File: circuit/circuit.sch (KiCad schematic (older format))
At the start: 8 parts

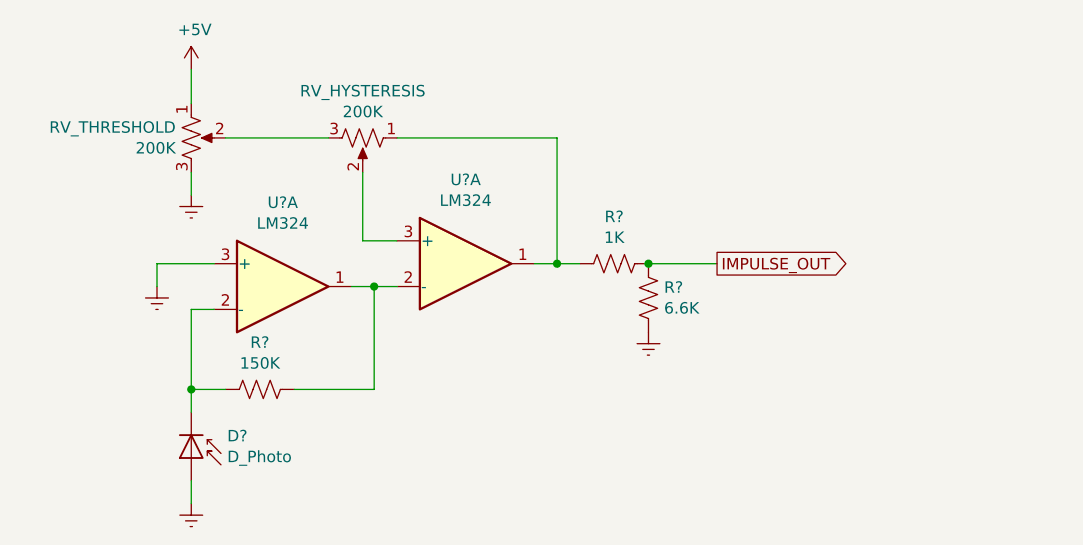
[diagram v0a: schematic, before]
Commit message: Update schematic.
Remove the hysteresis selection pot and change it to fixed 0.28v of hysteresis.
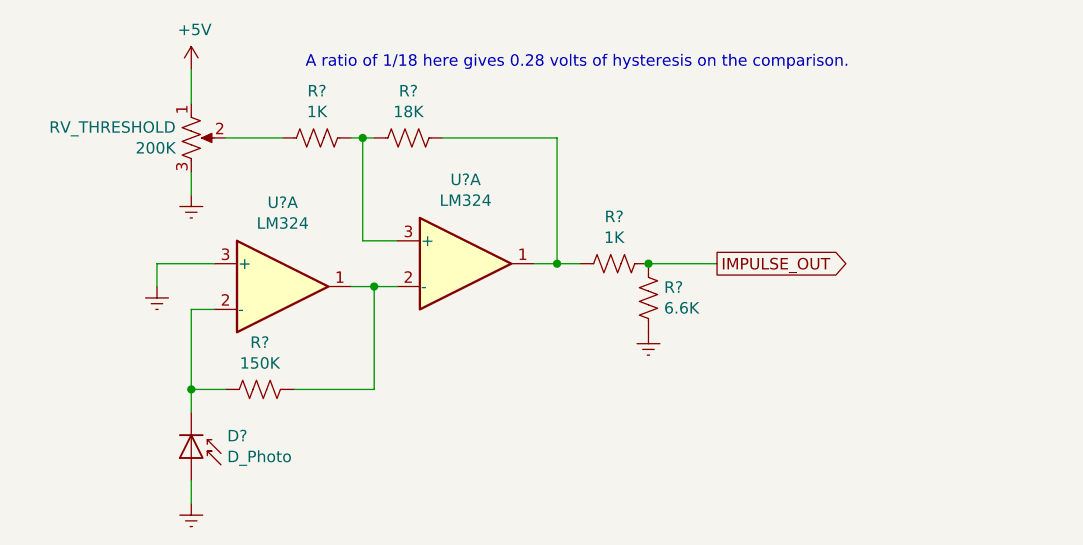
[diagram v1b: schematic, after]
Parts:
- removed RV_HYSTERESIS: 200K, symbol Device:R_POT_US
- added R?: 18K, symbol Device:R_US
- added R?: 1K, symbol Device:R_US
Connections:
- net at R?.2, U?.1: now also R?.2
- net at U?.3 (+): now also R?.1, R?.2
- net at RV_THRESHOLD.2: now also R?.1
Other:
- note added: "A ratio of 1/18 here gives 0.28 volts of hysteresis on the comparison."
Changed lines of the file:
@@
-$EndComp
-$Comp
-L Device:R_POT_US RV_HYSTERESIS
-U 1 1 61420C5A
-P 3700 1700
-F 0 "RV_HYSTERESIS" V 3495 1700 50  0000 C CNN
-F 1 "200K" V 3586 1700 50  0000 C CNN
-F 2 "" H 3700 1700 50  0001 C CNN
-F 3 "~" H 3700 1700 50  0001 C CNN
-	1    3700 1700
-	0    1    1    0
 $EndComp
 $Comp
@@
 	1    0    0    -1
 $EndComp
-Wire Wire Line
-	3100 1700 3550 1700
 $Comp
 L power:+5V #PWR?
@@
 	2950 1400 2950 1550
 Wire Wire Line
-	3850 1700 4550 1700
-Wire Wire Line
 	4550 1700 4550 2250
 Wire Wire Line
 	4550 2250 4450 2250
-Wire Wire Line
-	3700 1850 3700 2150
 Wire Wire Line
 	3700 2150 3850 2150
@@
 	3850 2350 3750 2350
 Connection ~ 3750 2350
+$Comp
+L Device:R_US R?
+U 1 1 61440E5A
+P 3900 1700
+F 0 "R?" V 4105 1700 50  0000 C CNN
+F 1 "18K" V 4014 1700 50  0000 C CNN
+F 2 "" V 3940 1690 50  0001 C CNN
+F 3 "~" H 3900 1700 50  0001 C CNN
+	1    3900 1700
+	0    -1   -1   0
+$EndComp
+Wire Wire Line
+	3700 1700 3700 2150
+$Comp
+L Device:R_US R?
+U 1 1 6144199F
+P 3500 1700
+F 0 "R?" V 3705 1700 50  0000 C CNN
+F 1 "1K" V 3614 1700 50  0000 C CNN
+F 2 "" V 3540 1690 50  0001 C CNN
+F 3 "~" H 3500 1700 50  0001 C CNN
+	1    3500 1700
+	0    -1   -1   0
+$EndComp
+Wire Wire Line
+	3650 1700 3700 1700
+Wire Wire Line
+	3700 1700 3750 1700
+Connection ~ 3700 1700
+Wire Wire Line
+	4050 1700 4550 1700
+Wire Wire Line
+	3350 1700 3100 1700
+Text Notes 3450 1400 0    50   ~ 0
+A ratio of 1/18 here gives 0.28 volts of hysteresis on the comparison.
 $EndSCHEMATC

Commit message: Add start of board layout
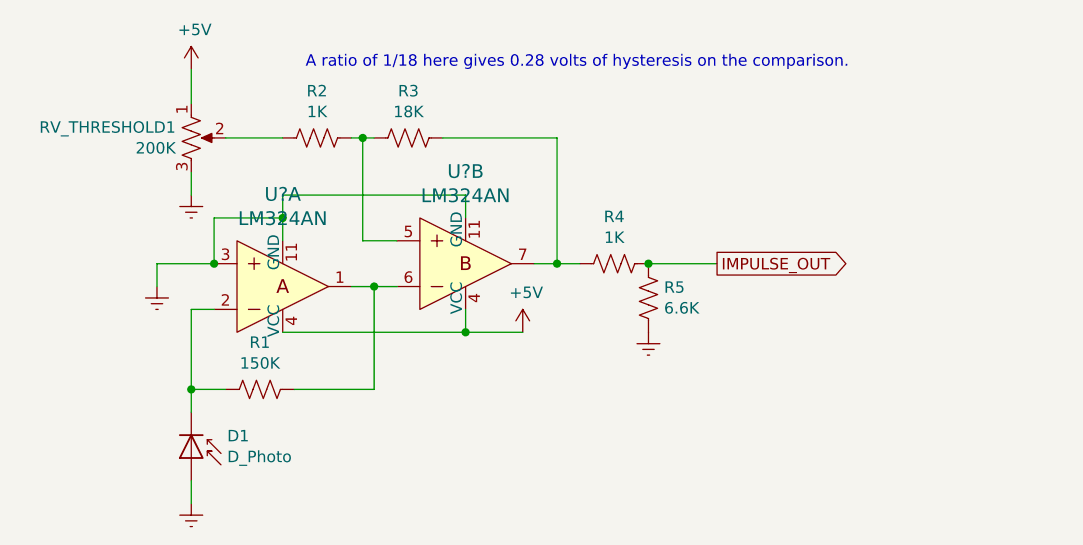
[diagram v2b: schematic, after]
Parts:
- removed U? (x2): LM324, symbol Amplifier_Operational:LM324
- added U? (x2): LM324AN, digikey-footprints:DIP-14_W3mm, symbol dk_Linear-Amplifiers-Instrumentation-OP-Amps-Buffer-Amps:LM324AN
- R1, R2, R3, R4, R5: renamed from R?; footprint (none) -> Resistor_THT:R_Axial_DIN0207_L6.3mm_D2.5mm_P10.16mm_Horizontal
- gave numbers to parts that had none: 1
- renumbered RV_THRESHOLD to RV_THRESHOLD1
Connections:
- net +5V: now also U?.4 (VCC), U?.4 (VCC)
- net Earth: now also U?.11 (GND), U?.11 (GND), U?.3
- net at R3.2, R4.2: now also U?.7
- net at R1.2: now also U?.1, U?.6
- net at R2.2, R3.1: now also U?.5
- net at D1.1 (K), R1.1: now also U?.2
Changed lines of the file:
@@
 $EndDescr
 $Comp
-L Amplifier_Operational:LM324 U?
-U 1 1 6141E584
-P 4150 2250
-F 0 "U?" H 4150 2617 50  0000 C CNN
-F 1 "LM324" H 4150 2526 50  0000 C CNN
-F 2 "" H 4100 2350 50  0001 C CNN
-F 3 "http://www.ti.com/lit/ds/symlink/lm2902-n.pdf" H 4200 2450 50  0001 C CNN
-	1    4150 2250
-	1    0    0    -1
-$EndComp
-$Comp
-L Device:R_POT_US RV_THRESHOLD
+L Device:R_POT_US RV_THRESHOLD1
 U 1 1 61422150
 P 2950 1700
-F 0 "RV_THRESHOLD" H 2882 1746 50  0000 R CNN
+F 0 "RV_THRESHOLD1" H 2882 1746 50  0000 R CNN
 F 1 "200K" H 2882 1655 50  0000 R CNN
 F 2 "" H 2950 1700 50  0001 C CNN
@@
 $EndComp
 $Comp
-L power:+5V #PWR?
+L power:+5V #PWR0101
 U 1 1 61423494
 P 2950 1400
-F 0 "#PWR?" H 2950 1250 50  0001 C CNN
+F 0 "#PWR0101" H 2950 1250 50  0001 C CNN
 F 1 "+5V" H 2965 1573 50  0000 C CNN
 F 2 "" H 2950 1400 50  0001 C CNN
@@
 $EndComp
 $Comp
-L power:Earth #PWR?
+L power:Earth #PWR0102
 U 1 1 6142409F
 P 2950 1950
-F 0 "#PWR?" H 2950 1700 50  0001 C CNN
+F 0 "#PWR0102" H 2950 1700 50  0001 C CNN
 F 1 "Earth" H 2950 1800 50  0001 C CNN
 F 2 "" H 2950 1950 50  0001 C CNN
@@
 Wire Wire Line
 	3700 2150 3850 2150
-$Comp
-L Amplifier_Operational:LM324 U?
-U 1 1 61425B46
-P 3350 2350
-F 0 "U?" H 3350 2717 50  0000 C CNN
-F 1 "LM324" H 3350 2626 50  0000 C CNN
-F 2 "" H 3300 2450 50  0001 C CNN
-F 3 "http://www.ti.com/lit/ds/symlink/lm2902-n.pdf" H 3400 2550 50  0001 C CNN
-	1    3350 2350
-	1    0    0    -1
-$EndComp
 Wire Wire Line
 	3650 2350 3750 2350
@@
 	2800 2250 2800 2350
 $Comp
-L power:Earth #PWR?
+L power:Earth #PWR0103
 U 1 1 61429E2B
 P 2800 2350
-F 0 "#PWR?" H 2800 2100 50  0001 C CNN
+F 0 "#PWR0103" H 2800 2100 50  0001 C CNN
 F 1 "Earth" H 2800 2200 50  0001 C CNN
 F 2 "" H 2800 2350 50  0001 C CNN
@@
 $EndComp
 $Comp
-L Device:R_US R?
+L Device:R_US R1
 U 1 1 6142A93A
 P 3250 2800
-F 0 "R?" V 3455 2800 50  0000 C CNN
+F 0 "R1" V 3455 2800 50  0000 C CNN
 F 1 "150K" V 3364 2800 50  0000 C CNN
-F 2 "" V 3290 2790 50  0001 C CNN
+F 2 "Resistor_THT:R_Axial_DIN0207_L6.3mm_D2.5mm_P10.16mm_Horizontal" V 3290 2790 50  0001 C CNN
 F 3 "~" H 3250 2800 50  0001 C CNN
 	1    3250 2800
@@
 	2950 2450 3050 2450
 $Comp
-L Device:D_Photo D?
+L Device:D_Photo D1
 U 1 1 6142C863
 P 2950 3100
-F 0 "D?" V 2854 3257 50  0000 L CNN
+F 0 "D1" V 2854 3257 50  0000 L CNN
 F 1 "D_Photo" V 2945 3257 50  0000 L CNN
 F 2 "" H 2900 3100 50  0001 C CNN
@@
 	2950 3200 2950 3300
 $Comp
-L power:Earth #PWR?
+L power:Earth #PWR0104
 U 1 1 6142D9DD
 P 2950 3300
-F 0 "#PWR?" H 2950 3050 50  0001 C CNN
+F 0 "#PWR0104" H 2950 3050 50  0001 C CNN
 F 1 "Earth" H 2950 3150 50  0001 C CNN
 F 2 "" H 2950 3300 50  0001 C CNN
@@
 $EndComp
 $Comp
-L Device:R_US R?
+L Device:R_US R4
 U 1 1 6142F1A5
 P 4800 2250
-F 0 "R?" V 4595 2250 50  0000 C CNN
+F 0 "R4" V 4595 2250 50  0000 C CNN
 F 1 "1K" V 4686 2250 50  0000 C CNN
-F 2 "" V 4840 2240 50  0001 C CNN
+F 2 "Resistor_THT:R_Axial_DIN0207_L6.3mm_D2.5mm_P10.16mm_Horizontal" V 4840 2240 50  0001 C CNN
 F 3 "~" H 4800 2250 50  0001 C CNN
 	1    4800 2250
@@
 $EndComp
 $Comp
-L Device:R_US R?
+L Device:R_US R5
 U 1 1 6142FDA4
 P 4950 2400
-F 0 "R?" H 4882 2354 50  0000 R CNN
+F 0 "R5" H 4882 2354 50  0000 R CNN
 F 1 "6.6K" H 4882 2445 50  0000 R CNN
-F 2 "" V 4990 2390 50  0001 C CNN
+F 2 "Resistor_THT:R_Axial_DIN0207_L6.3mm_D2.5mm_P10.16mm_Horizontal" V 4990 2390 50  0001 C CNN
 F 3 "~" H 4950 2400 50  0001 C CNN
 	1    4950 2400
@@
 $EndComp
 $Comp
-L power:Earth #PWR?
+L power:Earth #PWR0105
 U 1 1 6143068F
 P 4950 2550
-F 0 "#PWR?" H 4950 2300 50  0001 C CNN
+F 0 "#PWR0105" H 4950 2300 50  0001 C CNN
 F 1 "Earth" H 4950 2400 50  0001 C CNN
 F 2 "" H 4950 2550 50  0001 C CNN
@@
 Connection ~ 3750 2350
 $Comp
-L Device:R_US R?
+L Device:R_US R3
 U 1 1 61440E5A
 P 3900 1700
-F 0 "R?" V 4105 1700 50  0000 C CNN
+F 0 "R3" V 4105 1700 50  0000 C CNN
 F 1 "18K" V 4014 1700 50  0000 C CNN
-F 2 "" V 3940 1690 50  0001 C CNN
+F 2 "Resistor_THT:R_Axial_DIN0207_L6.3mm_D2.5mm_P10.16mm_Horizontal" V 3940 1690 50  0001 C CNN
 F 3 "~" H 3900 1700 50  0001 C CNN
 	1    3900 1700
@@
 	3700 1700 3700 2150
 $Comp
-L Device:R_US R?
+L Device:R_US R2
 U 1 1 6144199F
 P 3500 1700
-F 0 "R?" V 3705 1700 50  0000 C CNN
+F 0 "R2" V 3705 1700 50  0000 C CNN
 F 1 "1K" V 3614 1700 50  0000 C CNN
-F 2 "" V 3540 1690 50  0001 C CNN
+F 2 "Resistor_THT:R_Axial_DIN0207_L6.3mm_D2.5mm_P10.16mm_Horizontal" V 3540 1690 50  0001 C CNN
 F 3 "~" H 3500 1700 50  0001 C CNN
 	1    3500 1700
@@
 Text Notes 3450 1400 0    50   ~ 0
 A ratio of 1/18 here gives 0.28 volts of hysteresis on the comparison.
+$Comp
+L dk_Linear-Amplifiers-Instrumentation-OP-Amps-Buffer-Amps:LM324AN U?
+U 1 1 61447FCC
+P 3350 2350
+F 0 "U?" H 3350 1947 60  0000 C CNN
+F 1 "LM324AN" H 3350 2053 60  0000 C CNN
+F 2 "digikey-footprints:DIP-14_W3mm" H 3550 2550 60  0001 L CNN
+F 3 "http://www.ti.com/general/docs/suppproductinfo.tsp?distId=10&gotoUrl=http%3A%2F%2Fwww.ti.com%2Flit%2Fgpn%2Flm224" H 3550 2650 60  0001 L CNN
+F 4 "296-9542-5-ND" H 3550 2750 60  0001 L CNN "Digi-Key_PN"
+F 5 "LM324AN" H 3550 2850 60  0001 L CNN "MPN"
+F 6 "Integrated Circuits (ICs)" H 3550 2950 60  0001 L CNN "Category"
+F 7 "Linear - Amplifiers - Instrumentation, OP Amps, Buffer Amps" H 3550 3050 60  0001 L CNN "Family"
+F 8 "http://www.ti.com/general/docs/suppproductinfo.tsp?distId=10&gotoUrl=http%3A%2F%2Fwww.ti.com%2Flit%2Fgpn%2Flm224" H 3550 3150 60  0001 L CNN "DK_Datasheet_Link"
+F 9 "/product-detail/en/texas-instruments/LM324AN/296-9542-5-ND/412056" H 3550 3250 60  0001 L CNN "DK_Detail_Page"
+F 10 "IC OPAMP GP 4 CIRCUIT 14DIP" H 3550 3350 60  0001 L CNN "Description"
+F 11 "Texas Instruments" H 3550 3450 60  0001 L CNN "Manufacturer"
+F 12 "Active" H 3550 3550 60  0001 L CNN "Status"
+	1    3350 2350
+	1    0    0    1
+$EndComp
+Wire Wire Line
+	3350 2150 3350 2050
+Wire Wire Line
+	3350 2050 3050 2050
+Wire Wire Line
+	3050 2050 3050 2250
+Connection ~ 3050 2250
+$Comp
+L dk_Linear-Amplifiers-Instrumentation-OP-Amps-Buffer-Amps:LM324AN U?
+U 2 1 6144BF1C
+P 4150 2250
+F 0 "U?" H 4150 1847 60  0000 C CNN
+F 1 "LM324AN" H 4150 1953 60  0000 C CNN
+F 2 "digikey-footprints:DIP-14_W3mm" H 4350 2450 60  0001 L CNN
+F 3 "http://www.ti.com/general/docs/suppproductinfo.tsp?distId=10&gotoUrl=http%3A%2F%2Fwww.ti.com%2Flit%2Fgpn%2Flm224" H 4350 2550 60  0001 L CNN
+F 4 "296-9542-5-ND" H 4350 2650 60  0001 L CNN "Digi-Key_PN"
+F 5 "LM324AN" H 4350 2750 60  0001 L CNN "MPN"
+F 6 "Integrated Circuits (ICs)" H 4350 2850 60  0001 L CNN "Category"
+F 7 "Linear - Amplifiers - Instrumentation, OP Amps, Buffer Amps" H 4350 2950 60  0001 L CNN "Family"
+F 8 "http://www.ti.com/general/docs/suppproductinfo.tsp?distId=10&gotoUrl=http%3A%2F%2Fwww.ti.com%2Flit%2Fgpn%2Flm224" H 4350 3050 60  0001 L CNN "DK_Datasheet_Link"
+F 9 "/product-detail/en/texas-instruments/LM324AN/296-9542-5-ND/412056" H 4350 3150 60  0001 L CNN "DK_Detail_Page"
+F 10 "IC OPAMP GP 4 CIRCUIT 14DIP" H 4350 3250 60  0001 L CNN "Description"
+F 11 "Texas Instruments" H 4350 3350 60  0001 L CNN "Manufacturer"
+F 12 "Active" H 4350 3450 60  0001 L CNN "Status"
+	2    4150 2250
+	1    0    0    1
+$EndComp
+Wire Wire Line
+	3350 2550 4150 2550
+Wire Wire Line
+	4150 2550 4150 2450
+Wire Wire Line
+	4150 2050 4150 1950
+Wire Wire Line
+	4150 1950 3350 1950
+Wire Wire Line
+	3350 1950 3350 2050
+Connection ~ 3350 2050
+$Comp
+L power:+5V #PWR?
+U 1 1 61451173
+P 4400 2550
+F 0 "#PWR?" H 4400 2400 50  0001 C CNN
+F 1 "+5V" H 4415 2723 50  0000 C CNN
+F 2 "" H 4400 2550 50  0001 C CNN
+F 3 "" H 4400 2550 50  0001 C CNN
+	1    4400 2550
+	1    0    0    -1
+$EndComp
+Wire Wire Line
+	4150 2550 4400 2550
+Connection ~ 4150 2550
 $EndSCHEMATC
